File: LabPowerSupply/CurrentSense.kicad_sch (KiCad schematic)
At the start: 8 parts

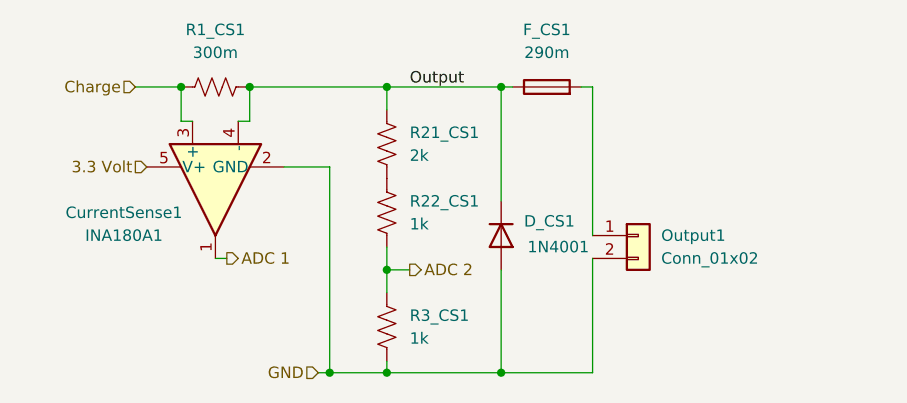
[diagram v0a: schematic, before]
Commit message: Screw terminals, routing
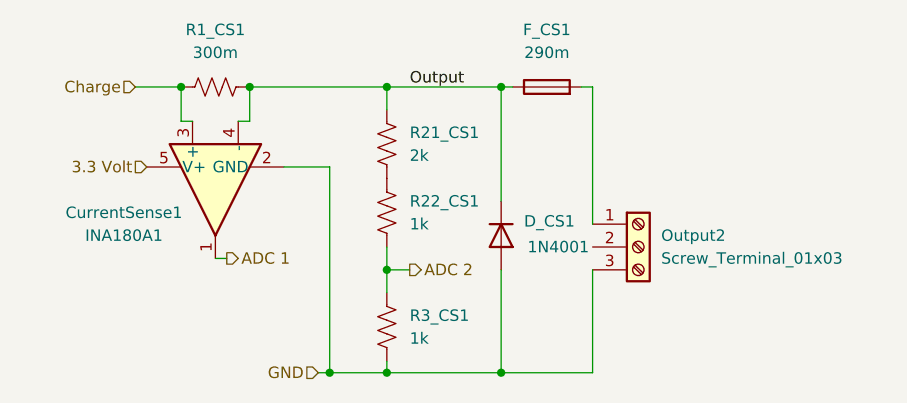
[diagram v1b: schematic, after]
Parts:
- removed Output1: Conn_01x02, Connector_Wire:SolderWire-2sqmm_1x02_P7.8mm_D2mm_OD3.9mm, symbol Connector_Generic:Conn_01x02
- added Output2: Screw_Terminal_01x03, TerminalBlock:TerminalBlock_Altech_AK300-3_P5.00mm, symbol Connector:Screw_Terminal_01x03
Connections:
- net GND: now also Output2.3 (Pin_3)
- net at F_CS1.2: now also Output2.1 (Pin_1)
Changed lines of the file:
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@@
     (stroke (width 0) (type default) (color 0 0 0 0))
   )
-  (wire (pts (xy 176.53 83.82) (xy 176.53 100.33))
+  (wire (pts (xy 176.53 83.82) (xy 176.53 99.06))
     (stroke (width 0) (type default) (color 0 0 0 0))
   )
@@
   )
   (wire (pts (xy 166.37 83.82) (xy 167.64 83.82))
+    (stroke (width 0) (type default) (color 0 0 0 0))
+  )
+  (wire (pts (xy 176.53 104.14) (xy 176.53 115.57))
     (stroke (width 0) (type default) (color 0 0 0 0))
   )
@@
   )
   (wire (pts (xy 142.24 92.71) (xy 147.32 92.71))
-    (stroke (width 0) (type default) (color 0 0 0 0))
-  )
-  (wire (pts (xy 176.53 102.87) (xy 176.53 115.57))
     (stroke (width 0) (type default) (color 0 0 0 0))
   )
@@
     (pin "5")
   )
-  (symbol (lib_id "Connector_Generic:Conn_01x02") (at 181.61 100.33 0) (unit 1)
-    (in_bom yes) (on_board yes)
-    (property "Reference" "Output1" (id 0) (at 184.15 100.3299 0)
-      (effects (font (size 1.27 1.27)) (justify left))
-    )
-    (property "Value" "Conn_01x02" (id 1) (at 184.15 102.87 0)
-      (effects (font (size 1.27 1.27)) (justify left))
-    )
-    (property "Footprint" "Connector_Wire:SolderWire-2sqmm_1x02_P7.8mm_D2mm_OD3.9mm" (id 2) (at 181.61 100.33 0)
-      (effects (font (size 1.27 1.27)) hide)
-    )
-    (property "Datasheet" "~" (id 3) (at 181.61 100.33 0)
-      (effects (font (size 1.27 1.27)) hide)
-    )
-    (pin "1")
-    (pin "2")
-  )
   (symbol (lib_id "Diode:1N4001") (at 166.37 100.33 270) (unit 1)
     (in_bom yes) (on_board yes)
@@
     (pin "2")
   )
+  (symbol (lib_id "Connector:Screw_Terminal_01x03") (at 181.61 101.6 0) (unit 1)
+    (in_bom yes) (on_board yes) (fields_autoplaced)
+    (property "Reference" "Output2" (id 0) (at 184.15 100.3299 0)
+      (effects (font (size 1.27 1.27)) (justify left))
+    )
+    (property "Value" "Screw_Terminal_01x03" (id 1) (at 184.15 102.8699 0)
+      (effects (font (size 1.27 1.27)) (justify left))
+    )
+    (property "Footprint" "TerminalBlock:TerminalBlock_Altech_AK300-3_P5.00mm" (id 2) (at 181.61 101.6 0)
+      (effects (font (size 1.27 1.27)) hide)
+    )
+    (property "Datasheet" "~" (id 3) (at 181.61 101.6 0)
+      (effects (font (size 1.27 1.27)) hide)
+    )
+    (pin "1")
+    (pin "2")
+    (pin "3")
+  )
   (symbol (lib_id "Device:R_US") (at 153.67 110.49 0) (unit 1)

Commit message: Fixed current sense and static modules
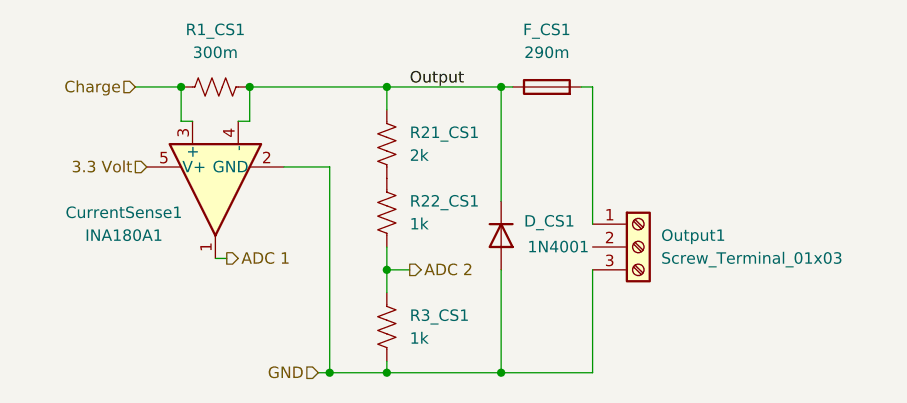
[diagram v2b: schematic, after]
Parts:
- R1_CS1: footprint Resistor_SMD:R_0603_1608Metric -> Resistor_SMD:R_1206_3216Metric
- renumbered Output2 to Output1
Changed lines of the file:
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@@
     (property "Reference" "R1_CS1" (id 0) (at 134.62 77.47 90))
     (property "Value" "300m" (id 1) (at 134.62 80.01 90))
-    (property "Footprint" "Resistor_SMD:R_0603_1608Metric" (id 2) (at 134.874 82.804 90)
+    (property "Footprint" "Resistor_SMD:R_1206_3216Metric" (id 2) (at 134.874 82.804 90)
       (effects (font (size 1.27 1.27)) hide)
     )
@@
   (symbol (lib_id "Connector:Screw_Terminal_01x03") (at 181.61 101.6 0) (unit 1)
     (in_bom yes) (on_board yes) (fields_autoplaced)
-    (property "Reference" "Output2" (id 0) (at 184.15 100.3299 0)
+    (property "Reference" "Output1" (id 0) (at 184.15 100.3299 0)
       (effects (font (size 1.27 1.27)) (justify left))
     )

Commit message: Extended ground fill
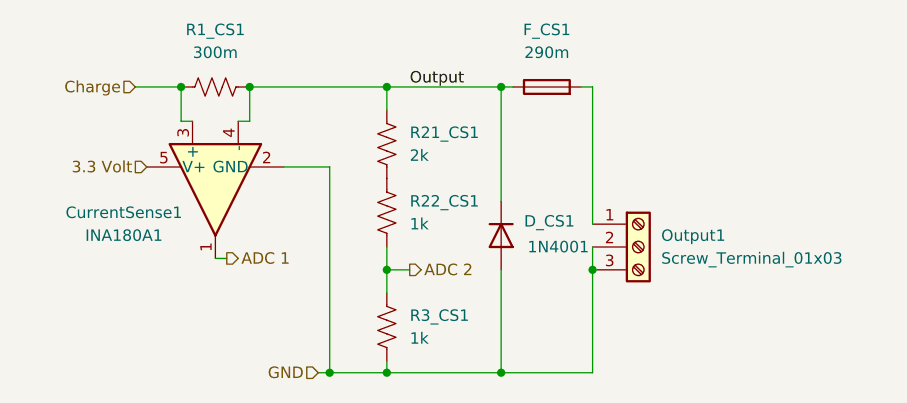
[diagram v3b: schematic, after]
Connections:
- net GND: now also Output1.2 (Pin_2)
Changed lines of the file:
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@@
   (junction (at 147.32 115.57) (diameter 0) (color 0 0 0 0)
+  )
+  (junction (at 176.53 104.14) (diameter 0) (color 0 0 0 0)
   )
   (junction (at 138.43 83.82) (diameter 0) (color 0 0 0 0)
@@
     (stroke (width 0) (type default) (color 0 0 0 0))
   )
+  (wire (pts (xy 176.53 101.6) (xy 176.53 104.14))
+    (stroke (width 0) (type default) (color 0 0 0 0))
+  )

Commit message: Began mcu placement
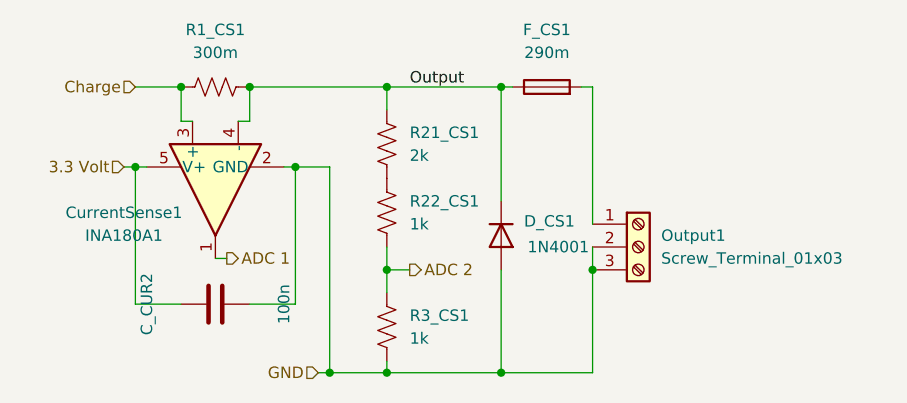
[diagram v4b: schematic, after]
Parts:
- added C_CUR2: 100n, Capacitor_SMD:C_0603_1608Metric, symbol Device:C
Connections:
- net 3.3 Volt: now also C_CUR2.2
- net GND: now also C_CUR2.1
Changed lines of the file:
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@@
   (junction (at 153.67 115.57) (diameter 0) (color 0 0 0 0)
   )
+  (junction (at 125.73 92.71) (diameter 0) (color 0 0 0 0)
+  )
   (junction (at 147.32 115.57) (diameter 0) (color 0 0 0 0)
   )
+  (junction (at 143.51 92.71) (diameter 0) (color 0 0 0 0)
+  )
   (junction (at 176.53 104.14) (diameter 0) (color 0 0 0 0)
   )
@@
     (stroke (width 0) (type default) (color 0 0 0 0))
   )
+  (wire (pts (xy 138.43 107.95) (xy 143.51 107.95))
+    (stroke (width 0) (type default) (color 0 0 0 0))
+  )
   (wire (pts (xy 176.53 83.82) (xy 176.53 99.06))
     (stroke (width 0) (type default) (color 0 0 0 0))
@@
     (stroke (width 0) (type default) (color 0 0 0 0))
   )
+  (wire (pts (xy 125.73 92.71) (xy 127 92.71))
+    (stroke (width 0) (type default) (color 0 0 0 0))
+  )
   (wire (pts (xy 166.37 104.14) (xy 166.37 115.57))
     (stroke (width 0) (type default) (color 0 0 0 0))
@@
     (stroke (width 0) (type default) (color 0 0 0 0))
   )
+  (wire (pts (xy 143.51 107.95) (xy 143.51 92.71))
+    (stroke (width 0) (type default) (color 0 0 0 0))
+  )
   (wire (pts (xy 166.37 83.82) (xy 167.64 83.82))
     (stroke (width 0) (type default) (color 0 0 0 0))
@@
     (stroke (width 0) (type default) (color 0 0 0 0))
   )
+  (wire (pts (xy 130.81 107.95) (xy 125.73 107.95))
+    (stroke (width 0) (type default) (color 0 0 0 0))
+  )
   (wire (pts (xy 153.67 83.82) (xy 153.67 86.36))
     (stroke (width 0) (type default) (color 0 0 0 0))
@@
     (stroke (width 0) (type default) (color 0 0 0 0))
   )
-  (wire (pts (xy 142.24 92.71) (xy 147.32 92.71))
+  (wire (pts (xy 142.24 92.71) (xy 143.51 92.71))
     (stroke (width 0) (type default) (color 0 0 0 0))
   )
@@
   )
   (wire (pts (xy 176.53 101.6) (xy 176.53 104.14))
+    (stroke (width 0) (type default) (color 0 0 0 0))
+  )
+  (wire (pts (xy 124.46 92.71) (xy 125.73 92.71))
+    (stroke (width 0) (type default) (color 0 0 0 0))
+  )
+  (wire (pts (xy 125.73 107.95) (xy 125.73 92.71))
+    (stroke (width 0) (type default) (color 0 0 0 0))
+  )
+  (wire (pts (xy 143.51 92.71) (xy 147.32 92.71))
     (stroke (width 0) (type default) (color 0 0 0 0))
   )
@@
     (effects (font (size 1.27 1.27)) (justify left))
   )
-  (hierarchical_label "3.3 Volt" (shape input) (at 127 92.71 180)
+  (hierarchical_label "3.3 Volt" (shape input) (at 124.46 92.71 180)
     (effects (font (size 1.27 1.27)) (justify right))
   )
@@
     (pin "3")
   )
+  (symbol (lib_id "Device:C") (at 134.62 107.95 270) (unit 1)
+    (in_bom yes) (on_board yes)
+    (property "Reference" "C_CUR2" (id 0) (at 127 107.95 0))
+    (property "Value" "100n" (id 1) (at 142.24 107.95 0))
+    (property "Footprint" "Capacitor_SMD:C_0603_1608Metric" (id 2) (at 130.81 108.9152 0)
+      (effects (font (size 1.27 1.27)) hide)
+    )
+    (property "Datasheet" "~" (id 3) (at 134.62 107.95 0)
+      (effects (font (size 1.27 1.27)) hide)
+    )
+    (pin "1")
+    (pin "2")
+  )
   (symbol (lib_id "Device:R_US") (at 153.67 110.49 0) (unit 1)

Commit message: Ch1 MCU placement
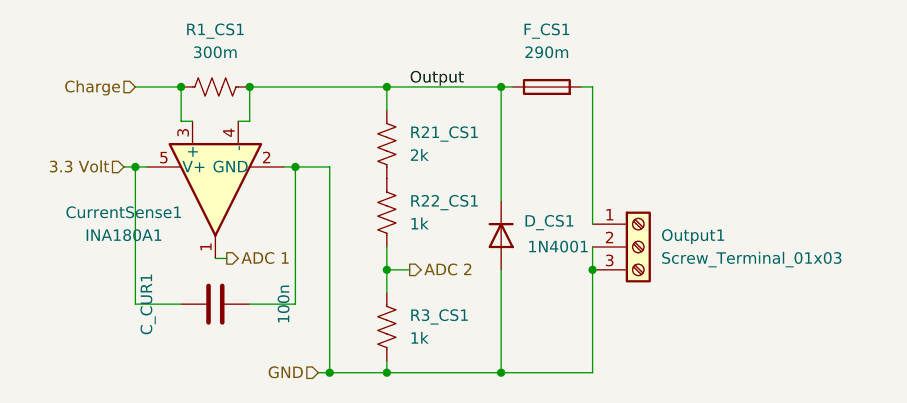
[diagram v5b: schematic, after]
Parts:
- renumbered C_CUR2 to C_CUR1
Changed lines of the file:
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@@
   (symbol (lib_id "Device:C") (at 134.62 107.95 270) (unit 1)
     (in_bom yes) (on_board yes)
-    (property "Reference" "C_CUR2" (id 0) (at 127 107.95 0))
+    (property "Reference" "C_CUR1" (id 0) (at 127 107.95 0))
     (property "Value" "100n" (id 1) (at 142.24 107.95 0))
     (property "Footprint" "Capacitor_SMD:C_0603_1608Metric" (id 2) (at 130.81 108.9152 0)

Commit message: Updated Part List
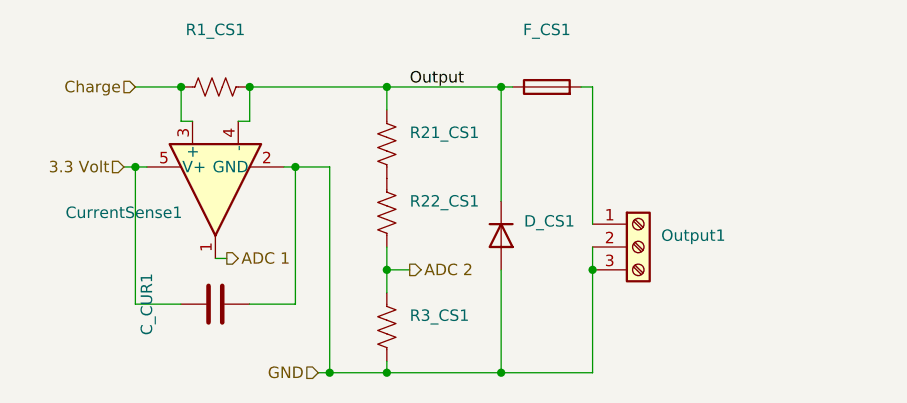
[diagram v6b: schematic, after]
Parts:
- C_CUR1: value 100n -> (none); footprint Capacitor_SMD:C_0603_1608Metric -> (none)
- CurrentSense1: value INA180A1 -> (none); footprint Package_TO_SOT_SMD:SOT-23-5 -> (none)
- D_CS1: value 1N4001 -> (none); footprint Diode_SMD:D_SMA -> (none)
- F_CS1: value 290m -> (none); footprint Fuse:Fuse_1812_4532Metric -> (none)
- Output1: value Screw_Terminal_01x03 -> (none); footprint TerminalBlock:TerminalBlock_Altech_AK300-3_P5.00mm -> (none)
- R1_CS1: value 300m -> (none); footprint Resistor_SMD:R_1206_3216Metric -> (none)
- R21_CS1: value 2k -> (none); footprint Resistor_SMD:R_0603_1608Metric -> (none)
- R22_CS1, R3_CS1: value 1k -> (none); footprint Resistor_SMD:R_0603_1608Metric -> (none)
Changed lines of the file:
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@@
       (effects (font (size 1.27 1.27)) (justify left))
     )
-    (property "Value" "1k" (id 1) (at 156.21 99.0599 0)
+    (property "Value" "" (id 1) (at 156.21 99.0599 0)
       (effects (font (size 1.27 1.27)) (justify left))
     )
-    (property "Footprint" "Resistor_SMD:R_0603_1608Metric" (id 2) (at 154.686 98.044 90)
+    (property "Footprint" "" (id 2) (at 154.686 98.044 90)
       (effects (font (size 1.27 1.27)) hide)
     )
@@
     (in_bom yes) (on_board yes) (fields_autoplaced)
     (property "Reference" "F_CS1" (id 0) (at 171.45 77.47 90))
-    (property "Value" "290m" (id 1) (at 171.45 80.01 90))
-    (property "Footprint" "Fuse:Fuse_1812_4532Metric" (id 2) (at 171.45 85.598 90)
+    (property "Value" "" (id 1) (at 171.45 80.01 90))
+    (property "Footprint" "" (id 2) (at 171.45 85.598 90)
       (effects (font (size 1.27 1.27)) hide)
     )
@@
     (in_bom yes) (on_board yes) (fields_autoplaced)
     (property "Reference" "R1_CS1" (id 0) (at 134.62 77.47 90))
-    (property "Value" "300m" (id 1) (at 134.62 80.01 90))
-    (property "Footprint" "Resistor_SMD:R_1206_3216Metric" (id 2) (at 134.874 82.804 90)
+    (property "Value" "" (id 1) (at 134.62 80.01 90))
+    (property "Footprint" "" (id 2) (at 134.874 82.804 90)
       (effects (font (size 1.27 1.27)) hide)
     )
@@
       (effects (font (size 1.27 1.27)) (justify left))
     )
-    (property "Value" "2k" (id 1) (at 156.21 91.4399 0)
+    (property "Value" "" (id 1) (at 156.21 91.4399 0)
       (effects (font (size 1.27 1.27)) (justify left))
     )
-    (property "Footprint" "Resistor_SMD:R_0603_1608Metric" (id 2) (at 154.686 90.424 90)
+    (property "Footprint" "" (id 2) (at 154.686 90.424 90)
       (effects (font (size 1.27 1.27)) hide)
     )
@@
     (in_bom yes) (on_board yes)
     (property "Reference" "CurrentSense1" (id 0) (at 124.46 97.79 90))
-    (property "Value" "INA180A1" (id 1) (at 124.46 100.33 90))
-    (property "Footprint" "Package_TO_SOT_SMD:SOT-23-5" (id 2) (at 133.35 96.52 0)
+    (property "Value" "" (id 1) (at 124.46 100.33 90))
+    (property "Footprint" "" (id 2) (at 133.35 96.52 0)
       (effects (font (size 1.27 1.27)) hide)
     )
@@
       (effects (font (size 1.27 1.27)) (justify left))
     )
-    (property "Value" "1N4001" (id 1) (at 172.72 101.6 90))
-    (property "Footprint" "Diode_SMD:D_SMA" (id 2) (at 161.925 100.33 0)
+    (property "Value" "" (id 1) (at 172.72 101.6 90))
+    (property "Footprint" "" (id 2) (at 161.925 100.33 0)
       (effects (font (size 1.27 1.27)) hide)
     )
@@
       (effects (font (size 1.27 1.27)) (justify left))
     )
-    (property "Value" "Screw_Terminal_01x03" (id 1) (at 184.15 102.8699 0)
+    (property "Value" "" (id 1) (at 184.15 102.8699 0)
       (effects (font (size 1.27 1.27)) (justify left))
     )
-    (property "Footprint" "TerminalBlock:TerminalBlock_Altech_AK300-3_P5.00mm" (id 2) (at 181.61 101.6 0)
+    (property "Footprint" "" (id 2) (at 181.61 101.6 0)
       (effects (font (size 1.27 1.27)) hide)
     )
@@
     (in_bom yes) (on_board yes)
     (property "Reference" "C_CUR1" (id 0) (at 127 107.95 0))
-    (property "Value" "100n" (id 1) (at 142.24 107.95 0))
-    (property "Footprint" "Capacitor_SMD:C_0603_1608Metric" (id 2) (at 130.81 108.9152 0)
+    (property "Value" "" (id 1) (at 142.24 107.95 0))
+    (property "Footprint" "" (id 2) (at 130.81 108.9152 0)
       (effects (font (size 1.27 1.27)) hide)
     )
@@
       (effects (font (size 1.27 1.27)) (justify left))
     )
-    (property "Value" "1k" (id 1) (at 156.21 111.7599 0)
+    (property "Value" "" (id 1) (at 156.21 111.7599 0)
       (effects (font (size 1.27 1.27)) (justify left))
     )
-    (property "Footprint" "Resistor_SMD:R_0603_1608Metric" (id 2) (at 154.686 110.744 90)
+    (property "Footprint" "" (id 2) (at 154.686 110.744 90)
       (effects (font (size 1.27 1.27)) hide)
     )
